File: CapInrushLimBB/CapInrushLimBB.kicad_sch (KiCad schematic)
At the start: 27 parts

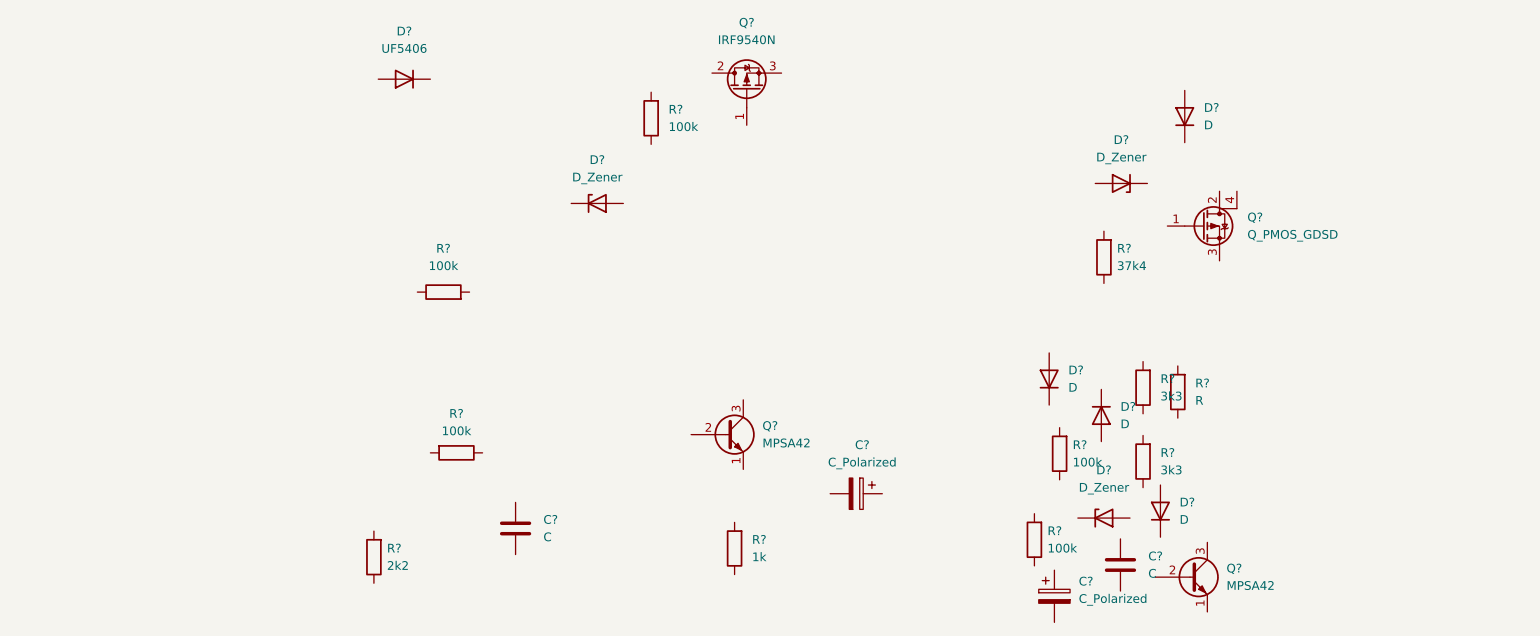
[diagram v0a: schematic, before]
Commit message: Connected up schematic prior to finalising component choice.
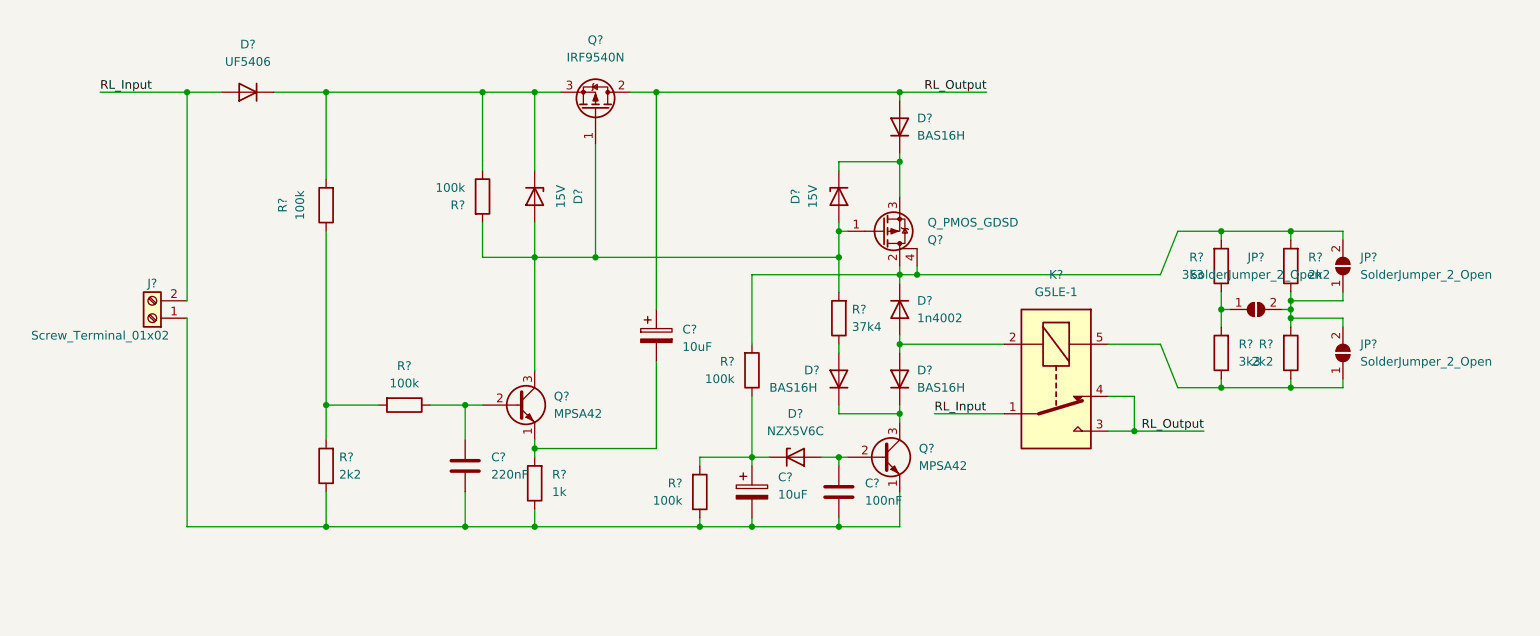
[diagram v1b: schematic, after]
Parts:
- removed D? (x2): D_Zener, symbol Device:D_Zener
- removed R?: 100k, symbol Device:R
- added D?: 15V, symbol Device:D_Zener
- added D?: NZX5V6C, symbol Device:D_Zener
- added J?: Screw_Terminal_01x02, TerminalBlock:TerminalBlock_Altech_AK300-2_P5.00mm, symbol Connector:Screw_Terminal_01x02
- added JP? (x3): SolderJumper_2_Open, symbol Jumper:SolderJumper_2_Open
- added K?: G5LE-1, Relay_THT:Relay_SPDT_Omron-G5LE-1, symbol Relay:G5LE-1
- added R?: 100k, symbol Device:R
- added R?: 2k2, symbol Device:R
- C? (x2): value C_Polarized -> 10uF
- C?: value C -> 220nF
- C?: value C -> 100nF
- D?: value D_Zener -> 15V
- D? (x3): value D -> BAS16H
- D?: value D -> 1n4002
- R?: value R -> 2k2
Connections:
- net at R?.1: now also R?.2, R?.2
- net at R?.2: now also D?.1 (K), D?.1 (K), Q?.3 (S), R?.1
- net at Q?.1 (G): now also D?.2 (A), Q?.1 (G), Q?.3 (C), R?.2, R?.2, D?.2 (A)
- net RL_Output: now reaches Q?.2 (D)
- net RL_Output: now also C?.1, D?.2 (A), K?.3, K?.4
- net at R?.1: now also C?.2, C?.2, C?.2, Q?.1 (E), R?.1, R?.1, J?.1 (Pin_1)
- net at D?.1 (K): now also Q?.3 (S), D?.1 (K)
- net at C?.2: now also Q?.1 (E), R?.2
- net at R?.1: now also D?.2 (A)
- net at R?.1: now also JP?.1 (A), JP?.2 (B), JP?.2 (B), R?.2
- net at R?.2: now also D?.1 (K), Q?.2 (D), Q?.4 (D), R?.2, JP?.2 (B), R?.2
- net at R?.1: now also C?.1, Q?.2 (B)
- net at R?.2: now also C?.1, D?.1 (K), R?.1
- net RL_Input: now reaches D?.2 (A)
- net RL_Input: now also J?.2 (Pin_2), K?.1
- net at R?.1: now also R?.2, JP?.1 (A)
- net at Q?.2 (B): now also C?.1, D?.2 (A)
- net at Q?.3 (C): now also D?.1 (K), D?.1 (K)
- net at R?.1: now also JP?.1 (A), K?.5, R?.1
- net at D?.2 (A): now also D?.2 (A), K?.2
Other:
- moved on the sheet: C?, D?, Q?, R?

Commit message: Updated component values/types (no footprints yet)
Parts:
- C?: value 10uF -> 10uF (715-3019)
- C?: value 220nF -> 220nF (in 188-6215 package)
- C?: value 100nF -> 100nF (653-0153)
- C?: value 10uF -> 10uF (440-6547)
- D? (x2): value 15V -> BZX79-C15
- D?: value UF5406 -> STPS10SM80CFP
- D?: value NZX5V6C -> BZX55C5V6
- R? (x2): value 3k3 -> 2k2
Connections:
- net RL_Output: no longer K?.4
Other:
- note added: "Pin 4 missing"
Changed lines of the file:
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@@
   (junction (at 63.5 119.38) (diameter 0) (color 0 0 0 0)
   )
-  (junction (at 181.61 123.19) (diameter 0) (color 0 0 0 0)
-  )
   (junction (at 138.43 127) (diameter 0) (color 0 0 0 0)
   )
@@
     (stroke (width 0) (type default) (color 0 0 0 0))
   )
-  (wire (pts (xy 181.61 123.19) (xy 191.77 123.19))
+  (wire (pts (xy 177.8 123.19) (xy 191.77 123.19))
     (stroke (width 0) (type default) (color 0 0 0 0))
   )
@@
     (stroke (width 0) (type default) (color 0 0 0 0))
   )
-  (wire (pts (xy 177.8 118.11) (xy 181.61 118.11))
-    (stroke (width 0) (type default) (color 0 0 0 0))
-  )
   (wire (pts (xy 194.31 102.87) (xy 194.31 105.41))
     (stroke (width 0) (type default) (color 0 0 0 0))
@@
     (stroke (width 0) (type default) (color 0 0 0 0))
   )
-  (wire (pts (xy 177.8 123.19) (xy 181.61 123.19))
-    (stroke (width 0) (type default) (color 0 0 0 0))
-  )
   (wire (pts (xy 138.43 135.89) (xy 138.43 137.16))
     (stroke (width 0) (type default) (color 0 0 0 0))
@@
     (stroke (width 0) (type default) (color 0 0 0 0))
   )
-  (wire (pts (xy 181.61 118.11) (xy 181.61 123.19))
-    (stroke (width 0) (type default) (color 0 0 0 0))
-  )
   (wire (pts (xy 187.96 116.84) (xy 194.31 116.84))
     (stroke (width 0) (type default) (color 0 0 0 0))
@@
   (wire (pts (xy 152.4 120.65) (xy 162.56 120.65))
     (stroke (width 0) (type default) (color 0 0 0 0))
+  )
+  (text "Pin 4 missing" (at 163.83 129.54 0)
+    (effects (font (size 1.27 1.27)) (justify left bottom))
   )
   (label "RL_Output" (at 160.02 73.66 180)
@@
     (in_bom yes) (on_board yes)
     (property "Reference" "D?" (id 0) (at 100.33 88.9 0))
-    (property "Value" "15V" (id 1) (at 97.79 88.9 0))
+    (property "Value" "BZX79-C15" (id 1) (at 97.79 88.9 0))
     (property "Footprint" "" (id 2) (at 93.98 88.9 0)
       (effects (font (size 1.27 1.27)) hide)
@@
       (effects (font (size 1.27 1.27)) (justify left))
     )
-    (property "Value" "10uF" (id 1) (at 115.57 110.8709 0)
+    (property "Value" "10uF (715-3019)" (id 1) (at 115.57 110.8709 0)
       (effects (font (size 1.27 1.27)) (justify left))
     )
@@
     (in_bom yes) (on_board yes)
     (property "Reference" "D?" (id 0) (at 132.08 88.9 0))
-    (property "Value" "15V" (id 1) (at 134.62 88.9 0))
+    (property "Value" "BZX79-C15" (id 1) (at 134.62 88.9 0))
     (property "Footprint" "" (id 2) (at 138.43 88.9 0)
       (effects (font (size 1.27 1.27)) hide)
@@
   (symbol (lib_id "Device:D") (at 52.07 73.66 180) (unit 1)
     (in_bom yes) (on_board yes) (fields_autoplaced)
-    (property "Reference" "D?" (id 0) (at 52.07 66.675 0))
-    (property "Value" "UF5406" (id 1) (at 52.07 69.215 0))
+    (property "Reference" "D?" (id 0) (at 52.07 67.31 0))
+    (property "Value" "STPS10SM80CFP" (id 1) (at 52.07 69.85 0))
     (property "Footprint" "" (id 2) (at 52.07 73.66 0)
       (effects (font (size 1.27 1.27)) hide)
@@
       (effects (font (size 1.27 1.27)) (justify right))
     )
-    (property "Value" "3k3" (id 1) (at 191.77 100.3299 0)
+    (property "Value" "2k2" (id 1) (at 191.77 100.3299 0)
       (effects (font (size 1.27 1.27)) (justify right))
     )
@@
       (effects (font (size 1.27 1.27)) (justify left))
     )
-    (property "Value" "220nF" (id 1) (at 87.63 129.5399 0)
+    (property "Value" "220nF (in 188-6215 package)" (id 1) (at 87.63 129.5399 0)
       (effects (font (size 1.27 1.27)) (justify left))
     )
@@
       (effects (font (size 1.27 1.27)) (justify right))
     )
-    (property "Value" "3k3" (id 1) (at 196.85 113.0299 0)
+    (property "Value" "2k2" (id 1) (at 196.85 113.0299 0)
       (effects (font (size 1.27 1.27)) (justify right))
     )
@@
       (effects (font (size 1.27 1.27)) (justify left))
     )
-    (property "Value" "100nF" (id 1) (at 142.24 133.3499 0)
+    (property "Value" "100nF (653-0153)" (id 1) (at 142.24 133.3499 0)
       (effects (font (size 1.27 1.27)) (justify left))
     )
@@
       (effects (font (size 1.27 1.27)) (justify left))
     )
-    (property "Value" "10uF" (id 1) (at 129.54 132.4609 0)
+    (property "Value" "10uF (440-6547)" (id 1) (at 129.54 132.4609 0)
       (effects (font (size 1.27 1.27)) (justify left))
     )
@@
     (in_bom yes) (on_board yes)
     (property "Reference" "D?" (id 0) (at 132.08 120.65 0))
-    (property "Value" "NZX5V6C" (id 1) (at 132.08 123.19 0))
+    (property "Value" "BZX55C5V6" (id 1) (at 132.08 123.19 0))
     (property "Footprint" "" (id 2) (at 132.08 127 0)
       (effects (font (size 1.27 1.27)) hide)
@@
   (symbol_instances
     (path "/4700c50c-9860-4532-a2c7-53fd9c745d97"
-      (reference "C?") (unit 1) (value "10uF") (footprint "")
+      (reference "C?") (unit 1) (value "10uF (715-3019)") (footprint "")
     )
     (path "/aa3000e9-ae89-4921-813a-5088ef73c282"
-      (reference "C?") (unit 1) (value "220nF") (footprint "")
+      (reference "C?") (unit 1) (value "220nF (in 188-6215 package)") (footprint "")
     )
     (path "/c42c87d9-6630-4bdd-b504-0fc4fcaddf1b"
-      (reference "C?") (unit 1) (value "100nF") (footprint "")
+      (reference "C?") (unit 1) (value "100nF (653-0153)") (footprint "")
     )
     (path "/d60a5db2-8cd8-4af1-8cbf-01714930ea15"
-      (reference "C?") (unit 1) (value "10uF") (footprint "")
+      (reference "C?") (unit 1) (value "10uF (440-6547)") (footprint "")
     )
     (path "/2420062a-7b05-40e0-a967-cfdef8a9ac4f"
-      (reference "D?") (unit 1) (value "15V") (footprint "")
+      (reference "D?") (unit 1) (value "BZX79-C15") (footprint "")
     )
     (path "/454ee090-04b0-4347-8b0f-a2f717ea927d"
@@
     )
     (path "/8b036306-9b43-4d58-90a3-f75924c14fc9"
-      (reference "D?") (unit 1) (value "15V") (footprint "")
+      (reference "D?") (unit 1) (value "BZX79-C15") (footprint "")
     )
     (path "/9b415808-d9bf-44e5-a529-91b246555e84"
-      (reference "D?") (unit 1) (value "UF5406") (footprint "")
+      (reference "D?") (unit 1) (value "STPS10SM80CFP") (footprint "")
     )
     (path "/b236afa7-5ddc-4fa0-8b38-6e2f2c55b1a6"
@@
     )
     (path "/f65a31ae-d1a6-44fe-9a57-5668cff0502e"
-      (reference "D?") (unit 1) (value "NZX5V6C") (footprint "")
+      (reference "D?") (unit 1) (value "BZX55C5V6") (footprint "")
     )
     (path "/670b39a3-baf9-475d-9b0c-feda51bc6306"
@@
     )
     (path "/a282ad8d-b833-4818-b5d4-3600a9280d0c"
-      (reference "R?") (unit 1) (value "3k3") (footprint "")
+      (reference "R?") (unit 1) (value "2k2") (footprint "")
     )
     (path "/aa761760-f24d-4b08-8605-6b8905e43edb"
-      (reference "R?") (unit 1) (value "3k3") (footprint "")
+      (reference "R?") (unit 1) (value "2k2") (footprint "")
     )
     (path "/f12d3516-d0d1-4859-ba7e-8885b73ae14c"

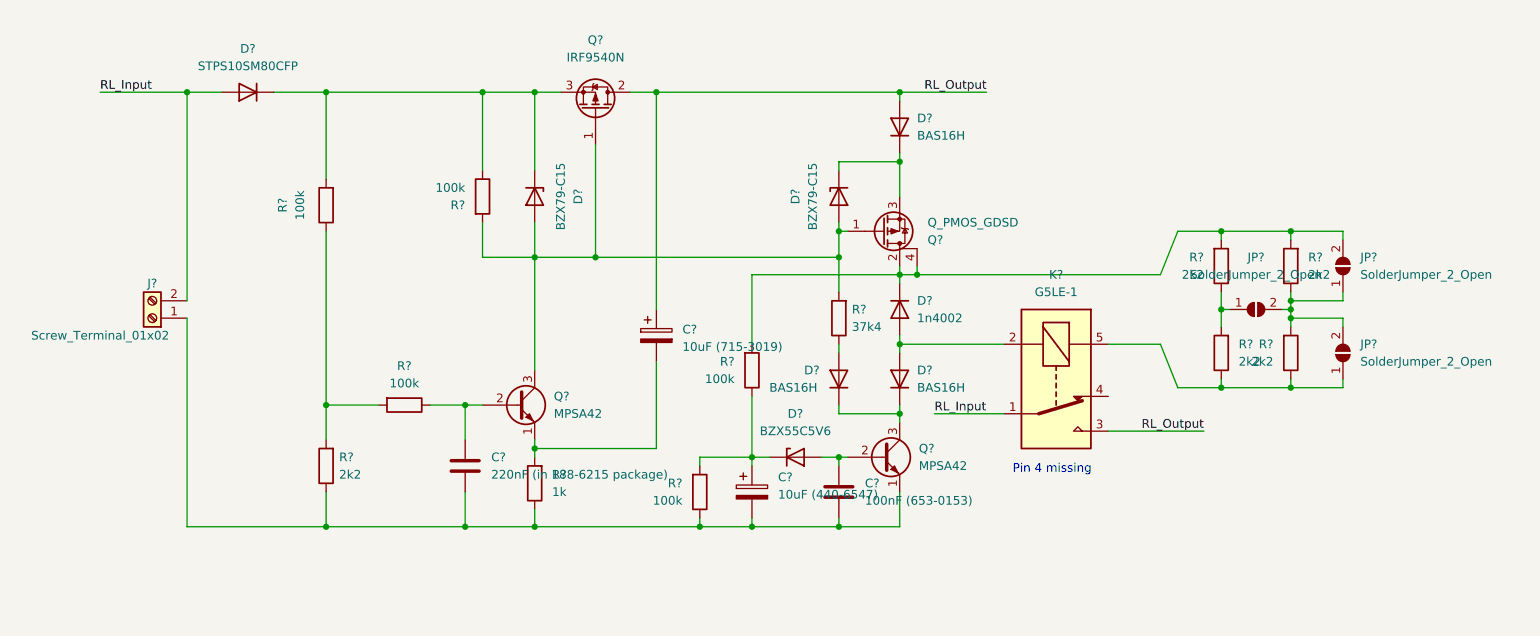
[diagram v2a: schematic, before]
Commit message: Tweaked layout in schematic.
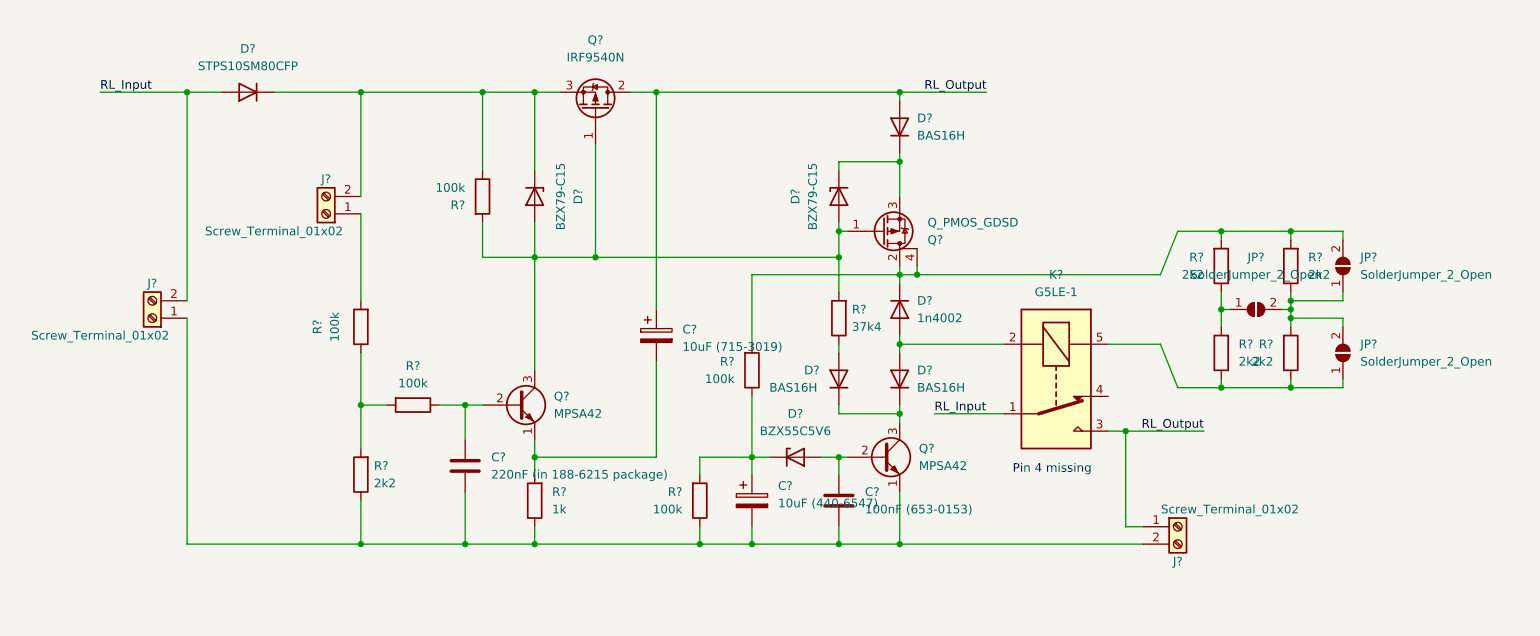
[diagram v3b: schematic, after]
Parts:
- added J? (x2): Screw_Terminal_01x02, TerminalBlock:TerminalBlock_Altech_AK300-2_P5.00mm, symbol Connector:Screw_Terminal_01x02
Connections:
- net RL_Output: now also J?.1 (Pin_1)
- net at D?.1 (K), D?.1 (K), Q?.3 (S)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: now also J?.2 (Pin_2); no longer R?.2
- net at C?.2, C?.2, C?.2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: now also J?.2 (Pin_2)
- new net: J?.1 (Pin_1), R?.2
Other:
- moved on the sheet: C?, R?

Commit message: Started footprint assignment.
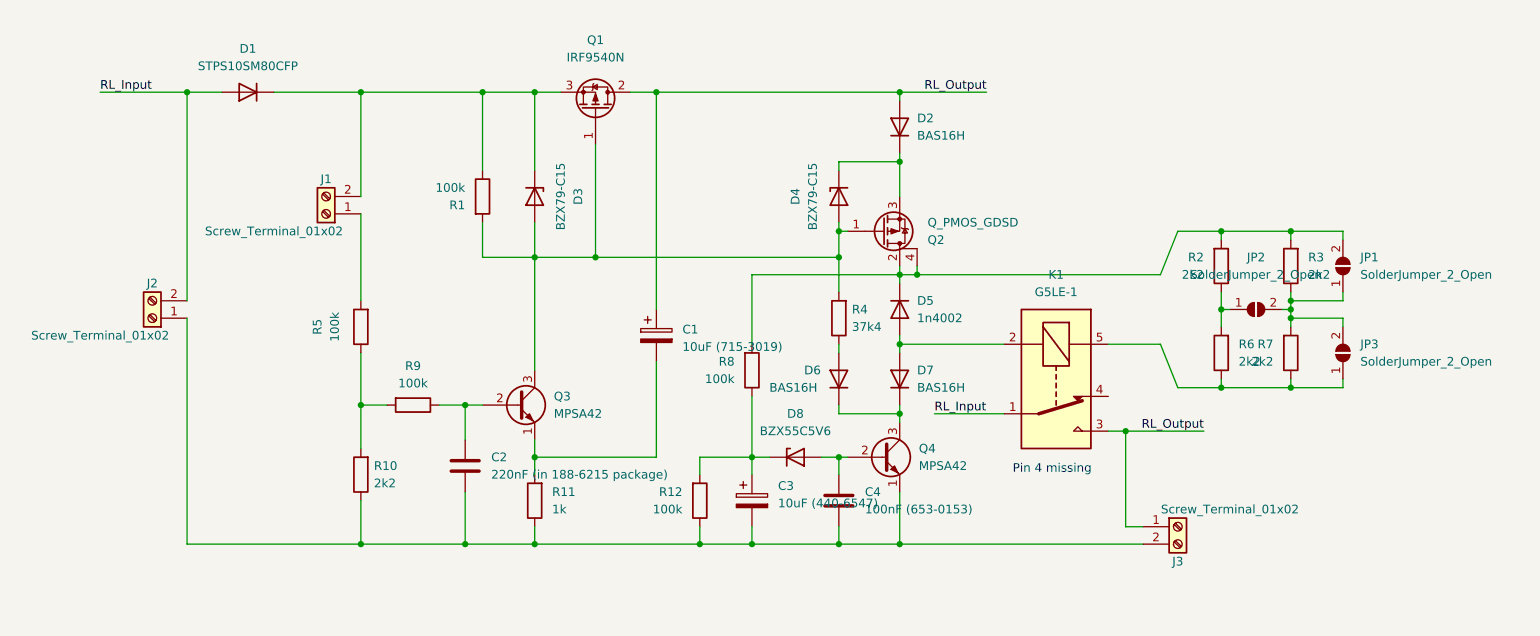
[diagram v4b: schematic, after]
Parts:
- C1: renamed from C?; footprint (none) -> Capacitor_THT:CP_Radial_D6.3mm_P2.50mm
- C2, C4: renamed from C?; footprint (none) -> Capacitor_THT:C_Disc_D5.1mm_W3.2mm_P5.00mm
- C3: renamed from C?; footprint (none) -> Capacitor_THT:CP_Radial_D5.0mm_P2.00mm
- gave numbers to parts that had none: 31

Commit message: Finished initial footprint assignment.
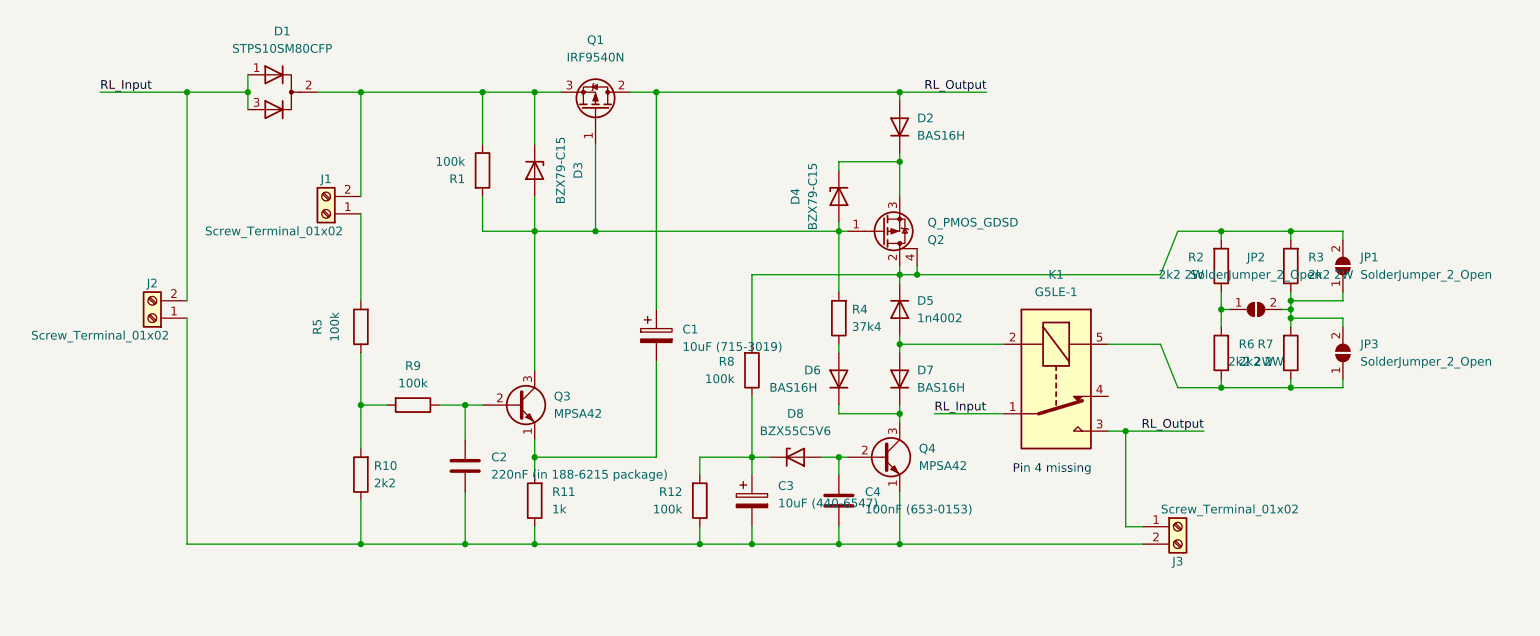
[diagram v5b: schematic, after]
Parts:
- removed D1: STPS10SM80CFP, symbol Device:D
- added D1: STPS10SM80CFP, Package_TO_SOT_THT:TO-220F-3_Vertical, symbol Device:D_Dual_CommonCathode_AKA_Parallel
- D2, D6, D7: footprint (none) -> Diode_SMD:D_SOD-323_HandSoldering
- D3, D4, D8: footprint (none) -> Diode_THT:D_DO-35_SOD27_P7.62mm_Horizontal
- D5: footprint (none) -> Diode_THT:D_DO-41_SOD81_P7.62mm_Horizontal
- JP1, JP2, JP3: footprint (none) -> Jumper:SolderJumper-2_P1.3mm_Open_Pad1.0x1.5mm
- Q2: footprint (none) -> Package_TO_SOT_SMD:SOT-223
- R1, R10, R11, R12, R4, R5, R8, R9: footprint (none) -> Resistor_THT:R_Axial_DIN0207_L6.3mm_D2.5mm_P7.62mm_Horizontal
- R2, R6: value 2k2 -> 2k2 2W; footprint (none) -> Resistor_THT:R_Axial_DIN0414_L11.9mm_D4.5mm_P20.32mm_Horizontal
- R3, R7: value 2k2 -> 2k2 2W; footprint (none) -> Resistor_THT:R_Axial_DIN0414_L11.9mm_D4.5mm_P15.24mm_Horizontal
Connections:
- net RL_Input: now also D1.1 (K), D1.3 (K)
- net at D3.1 (K), J1.2 (Pin_2), Q1.3 (S)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: now also D1.2 (A)
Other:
- moved on the sheet: D3, R1
